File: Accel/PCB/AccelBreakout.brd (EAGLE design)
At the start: 10.2 x 17.8 mm, 10 parts, among them U1 MMA8653FCR1

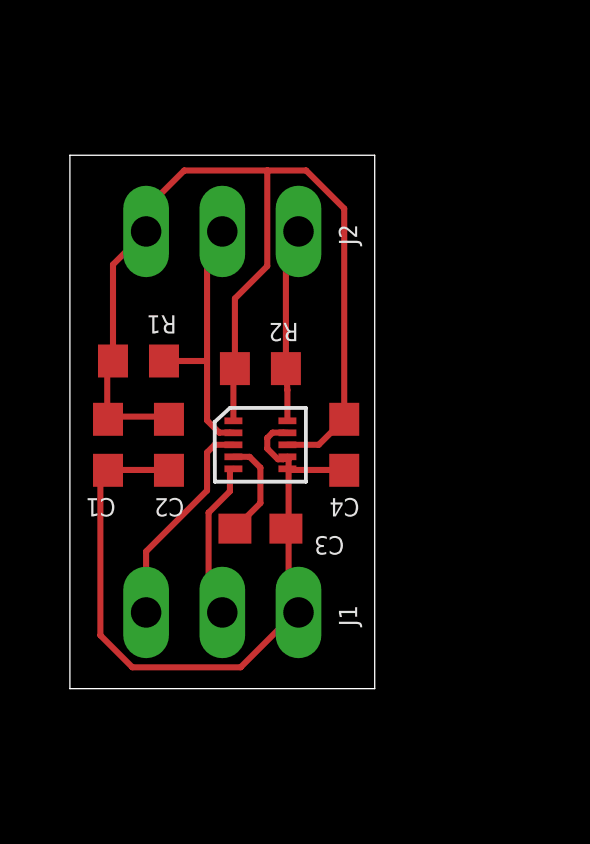
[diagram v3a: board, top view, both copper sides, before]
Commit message: accel - Added silkscreen copyright and rev
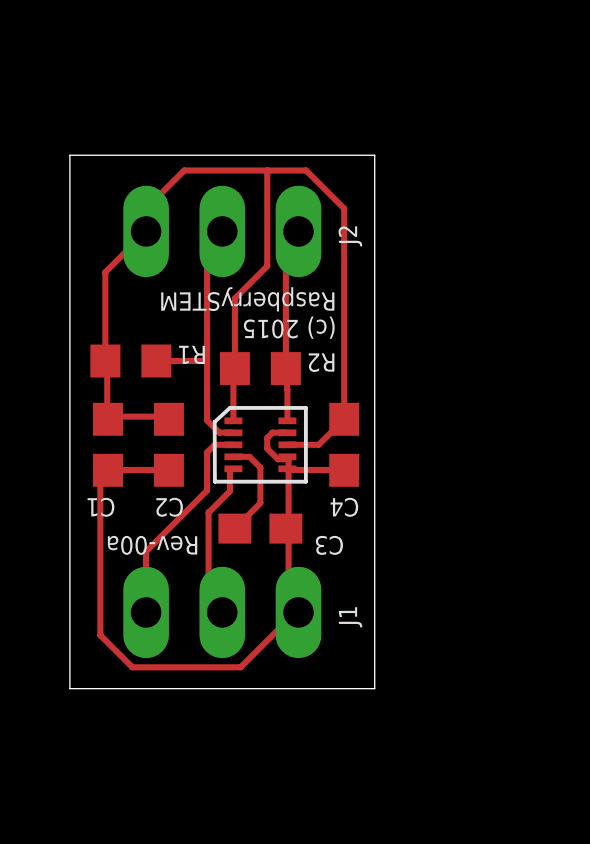
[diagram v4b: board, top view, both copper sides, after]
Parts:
- moved R1 0.25 mm to (2.03, 10.9)
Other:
- board text added: "(c) 2015 RaspberrySTEM"
- board text added: "Rev-00a"
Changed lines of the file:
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@@
 <layer number="14" name="Route14" color="1" fill="6" visible="no" active="no"/>
 <layer number="15" name="Route15" color="4" fill="6" visible="no" active="no"/>
-<layer number="16" name="Bottom" color="1" fill="1" visible="yes" active="yes"/>
+<layer number="16" name="Bottom" color="1" fill="1" visible="no" active="yes"/>
 <layer number="17" name="Pads" color="2" fill="1" visible="yes" active="yes"/>
 <layer number="18" name="Vias" color="2" fill="1" visible="yes" active="yes"/>
@@
 <layer number="20" name="Dimension" color="15" fill="1" visible="yes" active="yes"/>
 <layer number="21" name="tPlace" color="7" fill="1" visible="yes" active="yes"/>
-<layer number="22" name="bPlace" color="7" fill="1" visible="yes" active="yes"/>
+<layer number="22" name="bPlace" color="7" fill="1" visible="no" active="yes"/>
 <layer number="23" name="tOrigins" color="15" fill="1" visible="yes" active="yes"/>
-<layer number="24" name="bOrigins" color="15" fill="1" visible="yes" active="yes"/>
+<layer number="24" name="bOrigins" color="15" fill="1" visible="no" active="yes"/>
 <layer number="25" name="tNames" color="7" fill="1" visible="yes" active="yes"/>
-<layer number="26" name="bNames" color="7" fill="1" visible="yes" active="yes"/>
+<layer number="26" name="bNames" color="7" fill="1" visible="no" active="yes"/>
 <layer number="27" name="tValues" color="7" fill="1" visible="yes" active="yes"/>
-<layer number="28" name="bValues" color="7" fill="1" visible="yes" active="yes"/>
+<layer number="28" name="bValues" color="7" fill="1" visible="no" active="yes"/>
 <layer number="29" name="tStop" color="7" fill="3" visible="yes" active="yes"/>
-<layer number="30" name="bStop" color="7" fill="6" visible="yes" active="yes"/>
+<layer number="30" name="bStop" color="7" fill="6" visible="no" active="yes"/>
 <layer number="31" name="tCream" color="7" fill="4" visible="yes" active="yes"/>
 <layer number="32" name="bCream" color="7" fill="5" visible="yes" active="yes"/>
@@
 <text x="3.429" y="0.762" size="0.6096" layer="22" font="vector" rot="SMR180" align="bottom-right">INT1</text>
 <text x="5.969" y="0.762" size="0.6096" layer="22" font="vector" rot="SMR180" align="bottom-right">INT2</text>
+<text x="8.89" y="13.208" size="0.6096" layer="21" font="vector" rot="SR180">(c) 2015
+RaspberrySTEM</text>
+<text x="4.318" y="5.08" size="0.6096" layer="21" font="vector" rot="SR180">Rev-00a</text>
 </plain>
 <attributes>
@@
 <attribute name="NAME" x="9.652" y="6.35" size="0.6096" layer="25" font="vector" rot="SR180"/>
 </element>
-<element name="R1" library="resistor" package="R0603" value="10K" x="2.286" y="10.922" smashed="yes" rot="R180">
-<attribute name="NAME" x="3.556" y="12.446" size="0.6096" layer="25" font="vector" rot="SR180"/>
+<element name="R1" library="resistor" package="R0603" value="10K" x="2.032" y="10.922" smashed="yes" rot="R180">
+<attribute name="NAME" x="4.572" y="11.43" size="0.6096" layer="25" font="vector" rot="SR180"/>
 </element>
 <element name="R2" library="resistor" package="R0603" value="10K" x="6.35" y="10.668" smashed="yes" rot="R180">
-<attribute name="NAME" x="7.62" y="12.192" size="0.6096" layer="25" font="vector" rot="SR180"/>
+<attribute name="NAME" x="8.89" y="11.176" size="0.6096" layer="25" font="vector" rot="SR180"/>
 </element>
 <element name="J2" library="raspberrystem" package="1X03" value="" x="5.08" y="15.24" smashed="yes">
@@
 <wire x1="8.294" y1="8.128" x2="9.144" y2="8.978" width="0.2032" layer="1"/>
 <wire x1="1.2446" y1="9.0678" x2="1.2446" y2="10.9846" width="0.2032" layer="1"/>
-<wire x1="1.2446" y1="10.9846" x2="1.436" y2="10.922" width="0.2032" layer="1"/>
+<wire x1="1.2446" y1="10.9846" x2="1.182" y2="10.922" width="0.2032" layer="1"/>
 <wire x1="2.4892" y1="15.24" x2="2.54" y2="15.24" width="0.2032" layer="1"/>
-<wire x1="1.436" y1="10.922" x2="1.436" y2="14.136" width="0.2032" layer="1"/>
-<wire x1="1.436" y1="14.136" x2="2.54" y2="15.24" width="0.2032" layer="1"/>
+<wire x1="1.182" y1="10.922" x2="1.182" y2="13.882" width="0.2032" layer="1"/>
+<wire x1="1.182" y1="13.882" x2="2.54" y2="15.24" width="0.2032" layer="1"/>
 <wire x1="9.144" y1="8.978" x2="9.144" y2="16.002" width="0.2032" layer="1"/>
 <wire x1="9.144" y1="16.002" x2="7.874" y2="17.272" width="0.2032" layer="1"/>
@@
 <wire x1="4.572" y1="10.922" x2="4.572" y2="14.732" width="0.2032" layer="1"/>
 <wire x1="4.572" y1="14.732" x2="5.08" y2="15.24" width="0.2032" layer="1"/>
-<wire x1="3.136" y1="10.922" x2="4.572" y2="10.922" width="0.2032" layer="1"/>
+<wire x1="2.882" y1="10.922" x2="4.572" y2="10.922" width="0.2032" layer="1"/>
 </signal>
 <signal name="INT1">
@@
 </board>
 </drawing>
+<compatibility>
+<note version="6.3" minversion="6.2.2" severity="warning">
+Since Version 6.2.2 text objects can contain more than one line,
+which will not be processed correctly with this version.
+</note>
+</compatibility>
 </eagle>

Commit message: accel - Moved parts to local library (from raspberrystem.lbr)
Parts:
- J1, J2: device raspberrystem:1X03 -> AccelBreakout:1X03
- U1: device raspberrystem:MMA8653FCR1 -> AccelBreakout:MMA8653FCR1
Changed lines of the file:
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@@
 <layer number="56" name="wert" color="7" fill="1" visible="no" active="no"/>
 <layer number="57" name="tCAD" color="7" fill="1" visible="no" active="no"/>
+<layer number="90" name="Modules" color="5" fill="1" visible="no" active="no"/>
 <layer number="91" name="Nets" color="2" fill="1" visible="no" active="no"/>
 <layer number="92" name="Busses" color="1" fill="1" visible="no" active="no"/>
@@
 </autorouter>
 <elements>
-<element name="U1" library="raspberrystem" package="MMA8653FCR1" value="MMA8653FCR1" x="6.35" y="8.128"/>
+<element name="U1" library="AccelBreakout" package="MMA8653FCR1" value="MMA8653FCR1" x="6.35" y="8.128"/>
 <element name="C1" library="resistor" package="C0603" value="0.1uF" x="1.27" y="8.128" smashed="yes" rot="R270">
 <attribute name="NAME" x="1.524" y="6.35" size="0.6096" layer="25" font="vector" rot="SR180"/>
@@
 <attribute name="NAME" x="8.89" y="11.176" size="0.6096" layer="25" font="vector" rot="SR180"/>
 </element>
-<element name="J2" library="raspberrystem" package="1X03" value="" x="5.08" y="15.24" smashed="yes">
+<element name="J2" library="AccelBreakout" package="1X03" value="" x="5.08" y="15.24" smashed="yes">
 <attribute name="NAME" x="9.5758" y="14.7828" size="0.6096" layer="25" font="vector" ratio="10" rot="R90"/>
 <attribute name="VALUE" x="1.27" y="12.065" size="1.27" layer="27"/>
 </element>
-<element name="J1" library="raspberrystem" package="1X03" value="" x="5.08" y="2.54" smashed="yes">
+<element name="J1" library="AccelBreakout" package="1X03" value="" x="5.08" y="2.54" smashed="yes">
 <attribute name="NAME" x="9.5758" y="2.0828" size="0.6096" layer="25" font="vector" ratio="10" rot="R90"/>
 <attribute name="VALUE" x="1.27" y="-0.635" size="1.27" layer="27"/>

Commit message: accel - Fixed coordinate silkscreen label
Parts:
- removed U$2: (no value), raspberrystem:ACCEL_DIR
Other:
- board text added: "X"
- board text added: "Y"
- board text added: "Z"
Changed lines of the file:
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@@
 <layer number="14" name="Route14" color="1" fill="6" visible="no" active="no"/>
 <layer number="15" name="Route15" color="4" fill="6" visible="no" active="no"/>
-<layer number="16" name="Bottom" color="1" fill="1" visible="no" active="yes"/>
+<layer number="16" name="Bottom" color="1" fill="1" visible="yes" active="yes"/>
 <layer number="17" name="Pads" color="2" fill="1" visible="yes" active="yes"/>
 <layer number="18" name="Vias" color="2" fill="1" visible="yes" active="yes"/>
@@
 <layer number="20" name="Dimension" color="15" fill="1" visible="yes" active="yes"/>
 <layer number="21" name="tPlace" color="7" fill="1" visible="yes" active="yes"/>
-<layer number="22" name="bPlace" color="7" fill="1" visible="no" active="yes"/>
+<layer number="22" name="bPlace" color="7" fill="1" visible="yes" active="yes"/>
 <layer number="23" name="tOrigins" color="15" fill="1" visible="yes" active="yes"/>
-<layer number="24" name="bOrigins" color="15" fill="1" visible="no" active="yes"/>
+<layer number="24" name="bOrigins" color="15" fill="1" visible="yes" active="yes"/>
 <layer number="25" name="tNames" color="7" fill="1" visible="yes" active="yes"/>
-<layer number="26" name="bNames" color="7" fill="1" visible="no" active="yes"/>
+<layer number="26" name="bNames" color="7" fill="1" visible="yes" active="yes"/>
 <layer number="27" name="tValues" color="7" fill="1" visible="yes" active="yes"/>
-<layer number="28" name="bValues" color="7" fill="1" visible="no" active="yes"/>
+<layer number="28" name="bValues" color="7" fill="1" visible="yes" active="yes"/>
 <layer number="29" name="tStop" color="7" fill="3" visible="yes" active="yes"/>
-<layer number="30" name="bStop" color="7" fill="6" visible="no" active="yes"/>
+<layer number="30" name="bStop" color="7" fill="6" visible="yes" active="yes"/>
 <layer number="31" name="tCream" color="7" fill="4" visible="yes" active="yes"/>
 <layer number="32" name="bCream" color="7" fill="5" visible="yes" active="yes"/>
@@
 <wire x1="0" y1="17.78" x2="10.16" y2="17.78" width="0" layer="20"/>
 <wire x1="10.16" y1="17.78" x2="10.16" y2="0" width="0" layer="20"/>
-<text x="3.429" y="17.526" size="0.6096" layer="22" font="vector" rot="SMR180" align="bottom-right">VCC</text>
-<text x="8.509" y="0.762" size="0.6096" layer="22" font="vector" rot="SMR180" align="bottom-right">GND</text>
-<text x="8.509" y="17.526" size="0.6096" layer="22" font="vector" rot="SMR180" align="bottom-right">SDA</text>
-<text x="5.969" y="17.526" size="0.6096" layer="22" font="vector" rot="SMR180" align="bottom-right">SCL</text>
-<text x="3.429" y="0.762" size="0.6096" layer="22" font="vector" rot="SMR180" align="bottom-right">INT1</text>
-<text x="5.969" y="0.762" size="0.6096" layer="22" font="vector" rot="SMR180" align="bottom-right">INT2</text>
+<text x="3.429" y="17.526" size="0.6096" layer="22" font="vector" rot="MR180" align="bottom-right">VCC</text>
+<text x="8.509" y="0.762" size="0.6096" layer="22" font="vector" rot="MR180" align="bottom-right">GND</text>
+<text x="8.509" y="17.526" size="0.6096" layer="22" font="vector" rot="MR180" align="bottom-right">SDA</text>
+<text x="5.969" y="17.526" size="0.6096" layer="22" font="vector" rot="MR180" align="bottom-right">SCL</text>
+<text x="3.429" y="0.762" size="0.6096" layer="22" font="vector" rot="MR180" align="bottom-right">INT1</text>
+<text x="5.969" y="0.762" size="0.6096" layer="22" font="vector" rot="MR180" align="bottom-right">INT2</text>
 <text x="8.89" y="13.208" size="0.6096" layer="21" font="vector" rot="SR180">(c) 2015
 RaspberrySTEM</text>
 <text x="4.318" y="5.08" size="0.6096" layer="21" font="vector" rot="SR180">Rev-00a</text>
+<wire x1="1.397" y1="6.604" x2="3.048" y2="5.842" width="0.381" layer="22"/>
+<wire x1="1.397" y1="6.604" x2="3.048" y2="7.366" width="0.381" layer="22"/>
+<wire x1="6.858" y1="7.62" x2="6.858" y2="12.065" width="0.381" layer="22"/>
+<wire x1="6.858" y1="12.065" x2="6.096" y2="10.414" width="0.381" layer="22"/>
+<wire x1="6.858" y1="12.065" x2="7.62" y2="10.414" width="0.381" layer="22"/>
+<text x="0.762" y="7.366" size="1.27" layer="22" font="vector" rot="SMR0" align="bottom-right">X</text>
+<text x="5.08" y="11.557" size="1.27" layer="22" font="vector" rot="SMR0" align="bottom-right">Y</text>
+<circle x="6.858" y="6.604" radius="1.016" width="0.381" layer="22"/>
+<wire x1="5.842" y1="6.604" x2="1.397" y2="6.604" width="0.381" layer="22"/>
+<text x="8.382" y="5.461" size="1.27" layer="22" font="vector" rot="SMR0" align="bottom-right">Z</text>
+<circle x="6.858" y="6.604" radius="0.127" width="0.254" layer="22"/>
 </plain>
 <attributes>
@@
 <attribute name="VALUE" x="1.27" y="-0.635" size="1.27" layer="27"/>
 </element>
-<element name="U$2" library="raspberrystem" package="ACCEL_DIR" value="" x="6.858" y="10.922" rot="SR180"/>
 </elements>
 <signals>

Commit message: accel - silkscreen and board size changes
Box around R/Cs.  Increased board size to fit better pin labels
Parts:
- C1, C2, C3, C4: device resistor:C0603 -> AccelBreakout:C0603
- R1, R2: device resistor:R0603 -> AccelBreakout:R0603
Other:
- board size 10.2 x 17.8 mm -> 10.2 x 24.1 mm
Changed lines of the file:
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@@
 <setting verticaltext="up"/>
 </settings>
-<grid distance="100" unitdist="mil" unit="mil" style="lines" multiple="1" display="yes" altdistance="10" altunitdist="mil" altunit="mil"/>
+<grid distance="25" unitdist="mil" unit="mil" style="lines" multiple="1" display="yes" altdistance="5" altunitdist="mil" altunit="mil"/>
 <layers>
 <layer number="1" name="Top" color="4" fill="1" visible="yes" active="yes"/>
@@
 <board>
 <plain>
-<wire x1="10.16" y1="0" x2="0" y2="0" width="0" layer="20"/>
-<wire x1="0" y1="0" x2="0" y2="17.78" width="0" layer="20"/>
-<wire x1="0" y1="17.78" x2="10.16" y2="17.78" width="0" layer="20"/>
-<wire x1="10.16" y1="17.78" x2="10.16" y2="0" width="0" layer="20"/>
-<text x="3.429" y="17.526" size="0.6096" layer="22" font="vector" rot="MR180" align="bottom-right">VCC</text>
-<text x="8.509" y="0.762" size="0.6096" layer="22" font="vector" rot="MR180" align="bottom-right">GND</text>
-<text x="8.509" y="17.526" size="0.6096" layer="22" font="vector" rot="MR180" align="bottom-right">SDA</text>
-<text x="5.969" y="17.526" size="0.6096" layer="22" font="vector" rot="MR180" align="bottom-right">SCL</text>
-<text x="3.429" y="0.762" size="0.6096" layer="22" font="vector" rot="MR180" align="bottom-right">INT1</text>
-<text x="5.969" y="0.762" size="0.6096" layer="22" font="vector" rot="MR180" align="bottom-right">INT2</text>
+<wire x1="10.16" y1="-3.175" x2="0" y2="-3.175" width="0" layer="20"/>
+<wire x1="0" y1="-3.175" x2="0" y2="20.955" width="0" layer="20"/>
+<wire x1="0" y1="20.955" x2="10.16" y2="20.955" width="0" layer="20"/>
+<wire x1="10.16" y1="20.955" x2="10.16" y2="-3.175" width="0" layer="20"/>
+<text x="2.54" y="17.145" size="1.016" layer="22" font="vector" rot="MR90" align="center-left">VCC</text>
+<text x="7.62" y="0.635" size="1.016" layer="22" font="vector" rot="MR270" align="center-left">GND</text>
+<text x="7.62" y="17.145" size="1.016" layer="22" font="vector" rot="MR90" align="center-left">SDA</text>
+<text x="5.08" y="17.145" size="1.016" layer="22" font="vector" rot="MR90" align="center-left">SCL</text>
+<text x="2.54" y="0.635" size="1.016" layer="22" font="vector" rot="MR270" align="center-left">INT1</text>
+<text x="5.08" y="0.635" size="1.016" layer="22" font="vector" rot="MR270" align="center-left">INT2</text>
 <text x="8.89" y="13.208" size="0.6096" layer="21" font="vector" rot="SR180">(c) 2015
 RaspberrySTEM</text>
-<text x="4.318" y="5.08" size="0.6096" layer="21" font="vector" rot="SR180">Rev-00a</text>
+<text x="1.016" y="1.27" size="0.6096" layer="21" font="vector" rot="SR90">Rev-00a</text>
 <wire x1="1.397" y1="6.604" x2="3.048" y2="5.842" width="0.381" layer="22"/>
 <wire x1="1.397" y1="6.604" x2="3.048" y2="7.366" width="0.381" layer="22"/>
@@
 <elements>
 <element name="U1" library="AccelBreakout" package="MMA8653FCR1" value="MMA8653FCR1" x="6.35" y="8.128"/>
-<element name="C1" library="resistor" package="C0603" value="0.1uF" x="1.27" y="8.128" smashed="yes" rot="R270">
+<element name="C1" library="AccelBreakout" package="C0603" value="0.1uF" x="1.27" y="8.128" smashed="yes" rot="R270">
 <attribute name="NAME" x="1.524" y="6.35" size="0.6096" layer="25" font="vector" rot="SR180"/>
 </element>
-<element name="C2" library="resistor" package="C0603" value="1uF" x="3.302" y="8.128" smashed="yes" rot="R270">
+<element name="C2" library="AccelBreakout" package="C0603" value="1uF" x="3.302" y="8.128" smashed="yes" rot="R270">
 <attribute name="NAME" x="3.81" y="6.35" size="0.6096" layer="25" font="vector" rot="SR180"/>
 </element>
-<element name="C3" library="resistor" package="C0603" value="0.1uF" x="6.35" y="5.334" smashed="yes">
+<element name="C3" library="AccelBreakout" package="C0603" value="0.1uF" x="6.35" y="5.334" smashed="yes">
 <attribute name="NAME" x="9.144" y="5.08" size="0.6096" layer="25" font="vector" rot="SR180"/>
 </element>
-<element name="C4" library="resistor" package="C0603" value="0.1uF" x="9.144" y="8.128" smashed="yes" rot="R270">
+<element name="C4" library="AccelBreakout" package="C0603" value="0.1uF" x="9.144" y="8.128" smashed="yes" rot="R270">
 <attribute name="NAME" x="9.652" y="6.35" size="0.6096" layer="25" font="vector" rot="SR180"/>
 </element>
-<element name="R1" library="resistor" package="R0603" value="10K" x="2.032" y="10.922" smashed="yes" rot="R180">
-<attribute name="NAME" x="4.572" y="11.43" size="0.6096" layer="25" font="vector" rot="SR180"/>
-</element>
-<element name="R2" library="resistor" package="R0603" value="10K" x="6.35" y="10.668" smashed="yes" rot="R180">
-<attribute name="NAME" x="8.89" y="11.176" size="0.6096" layer="25" font="vector" rot="SR180"/>
+<element name="R1" library="AccelBreakout" package="R0603" value="10K" x="2.032" y="10.922" smashed="yes" rot="R180">
+<attribute name="NAME" x="1.27" y="12.573" size="0.6096" layer="25" font="vector" rot="SR180"/>
+</element>
+<element name="R2" library="AccelBreakout" package="R0603" value="10K" x="6.35" y="10.668" smashed="yes" rot="R180">
+<attribute name="NAME" x="9.271" y="11.43" size="0.6096" layer="25" font="vector" rot="SR180"/>
 </element>
 <element name="J2" library="AccelBreakout" package="1X03" value="" x="5.08" y="15.24" smashed="yes">
